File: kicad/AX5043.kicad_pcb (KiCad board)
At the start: 2 copper layers, 43 x 34 mm, 29 parts, among them U1 AX5043, X1 12.000MHz, X2 SMA

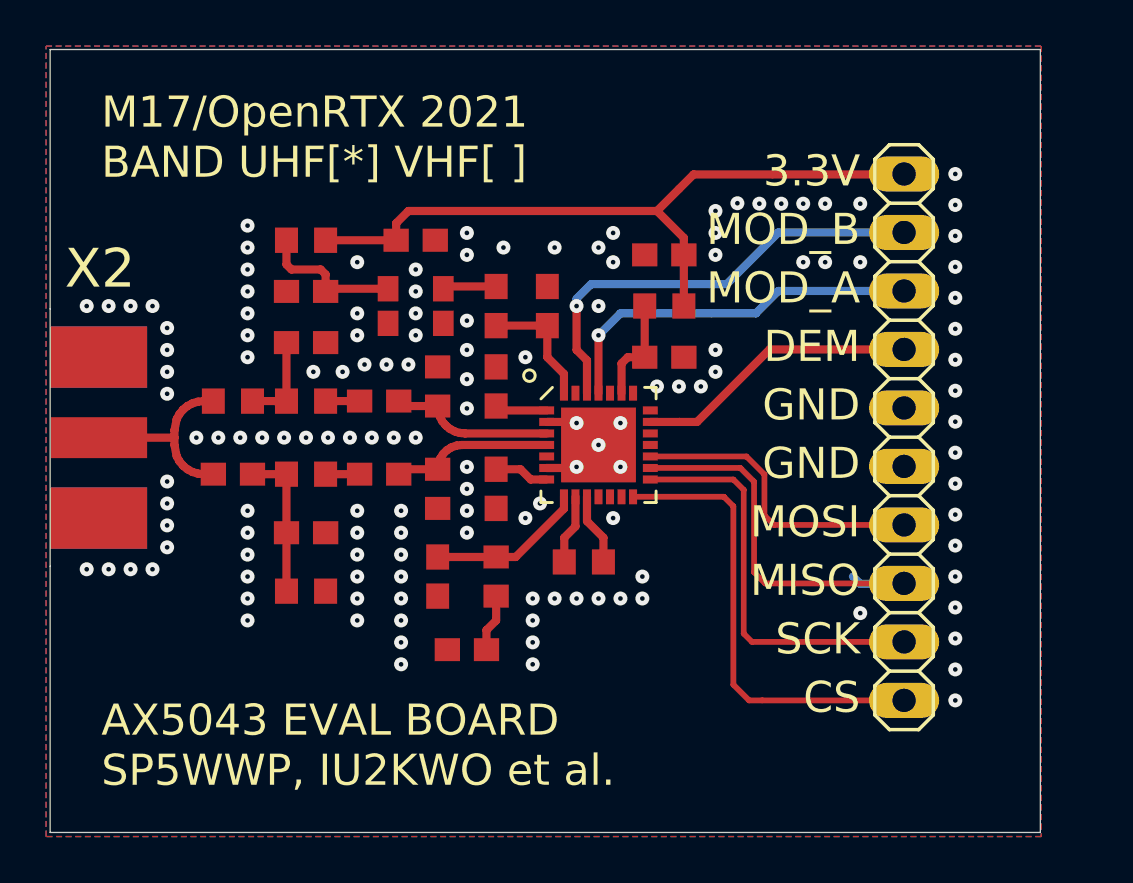
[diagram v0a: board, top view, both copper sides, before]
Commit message: Add rounded corners
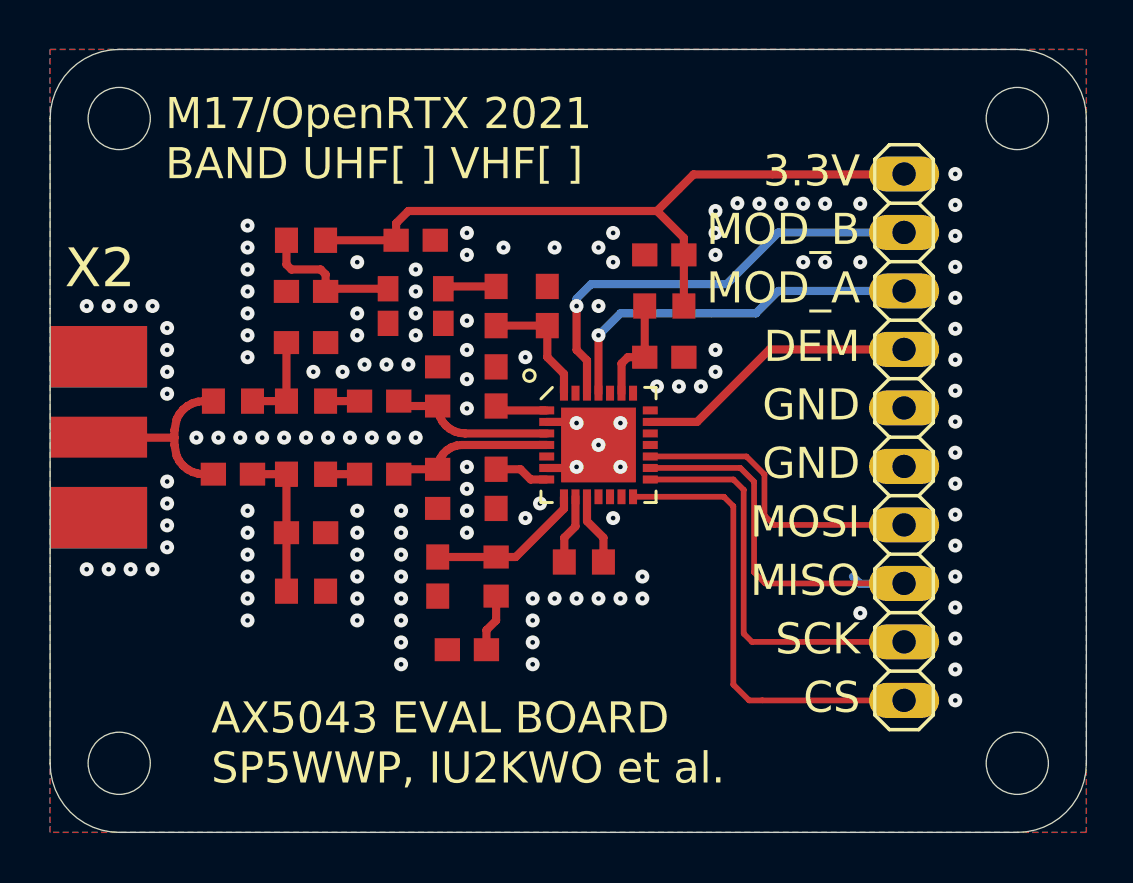
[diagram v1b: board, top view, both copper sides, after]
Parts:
- added REF**: MountingHole_2.7mm_M2.5, MountingHole:MountingHole_2.7mm_M2.5, F.Cu at (169.0, 119.0)
- added REF**: MountingHole_2.7mm_M2.5, MountingHole:MountingHole_2.7mm_M2.5, F.Cu at (169.0, 91.0)
- added REF**: MountingHole_2.7mm_M2.5, MountingHole:MountingHole_2.7mm_M2.5, F.Cu at (130.0, 119.0)
- added REF**: MountingHole_2.7mm_M2.5, MountingHole:MountingHole_2.7mm_M2.5, F.Cu at (130.0, 91.0)
- JP1: value (none) -> PINHD-1X10
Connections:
- R4 pad 1: Net-(R4-Pad1) -> Net-(C6-Pad2)
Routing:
- net GND: vias 125 -> 117
- net (no net): vias 12 -> 20
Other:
- board size 43 x 34 mm -> 45 x 34 mm
- board text added: "M17/OpenRTX 2021 BAND UHF[ ] VHF[ ]"
- board text removed: "M17/OpenRTX 2021 BAND UHF[*] VHF[ ]"

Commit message: Reorganised KiCad libraries
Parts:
- C1, C10, C11, C12, C13, C14, C15, C2, C3, C4, C5, C6, C7, C8, C9: footprint main:C0603 -> AX5043:C0603
- JP1: footprint main:1X10 -> AX5043:1X10
- R1, R10, R2, R3, R4, R5, R6, R7, R8, R9: footprint main:R0603 -> AX5043:R0603
- U1: footprint main:QFN28-5X5-WITH-CENTER-PAD -> AX5043:QFN28-5X5-WITH-CENTER-PAD
- X1: footprint main:ASE -> AX5043:ASE
- X2: footprint main:J502-ND-142-0711-821_826 -> AX5043:J502-ND-142-0711-821_826

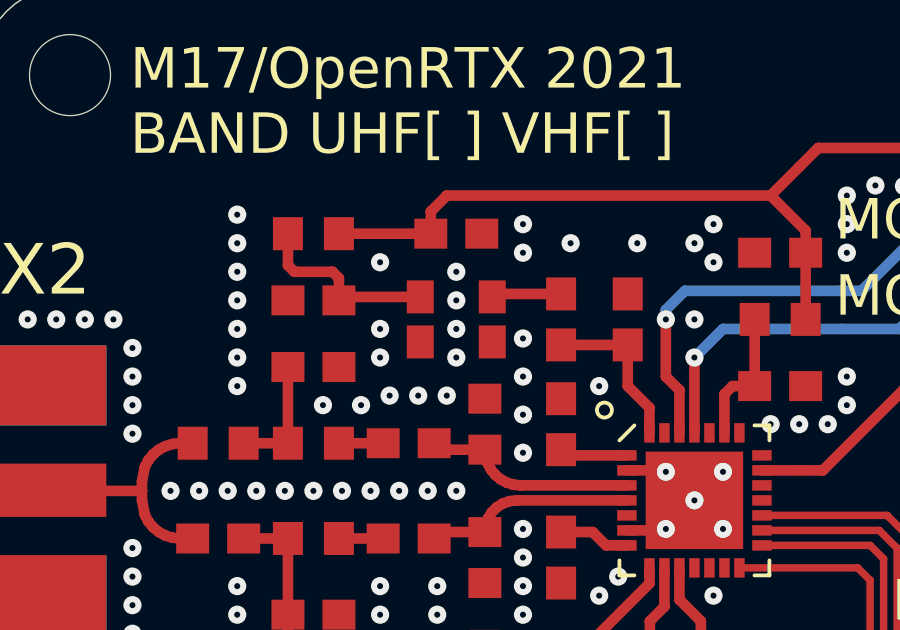
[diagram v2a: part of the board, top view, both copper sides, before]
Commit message: New footprint for TCXO, model is ECS-TXO-2520
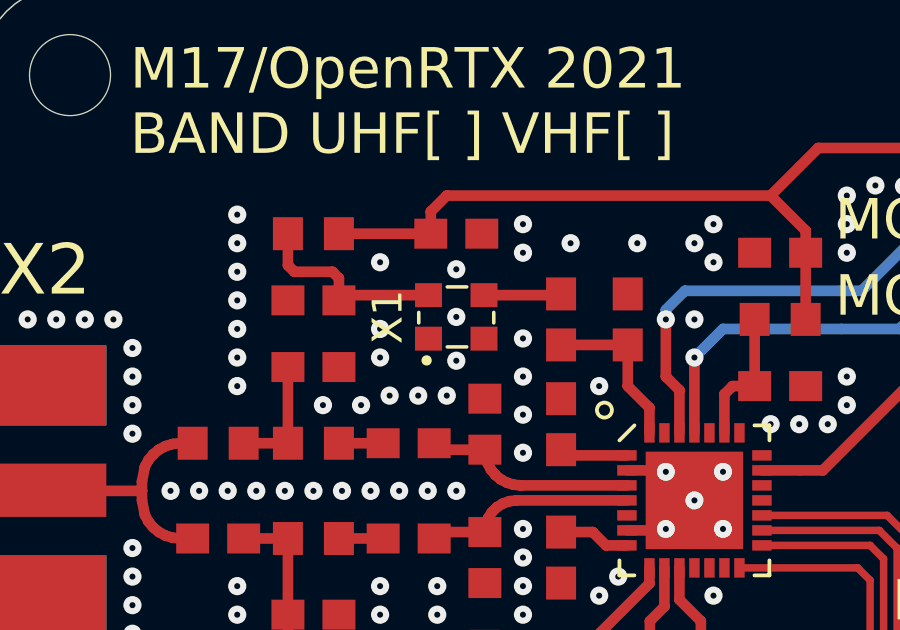
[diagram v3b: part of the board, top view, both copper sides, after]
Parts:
- X1: footprint AX5043:ASE -> AX5043:ECS-TXO-2520
- moved X1 0.08 mm to (142.9, 99.1), turned to 180 degrees
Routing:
- net GND: vias 117 -> 116

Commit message: Gerber files for PCB manufacturing
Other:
- board text added: "M17/OpenRTX 2021 v1.0 BAND UHF[ ] VHF[ ]"
- board text removed: "M17/OpenRTX 2021 BAND UHF[ ] VHF[ ]"

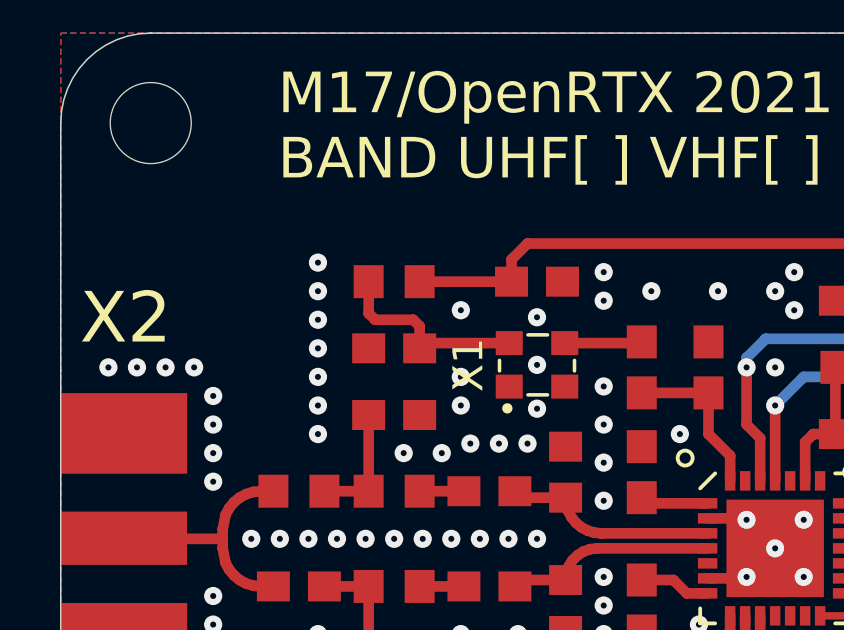
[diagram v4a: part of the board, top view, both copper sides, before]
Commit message: Fixed some unconnected ground vias, re-generated gerber files
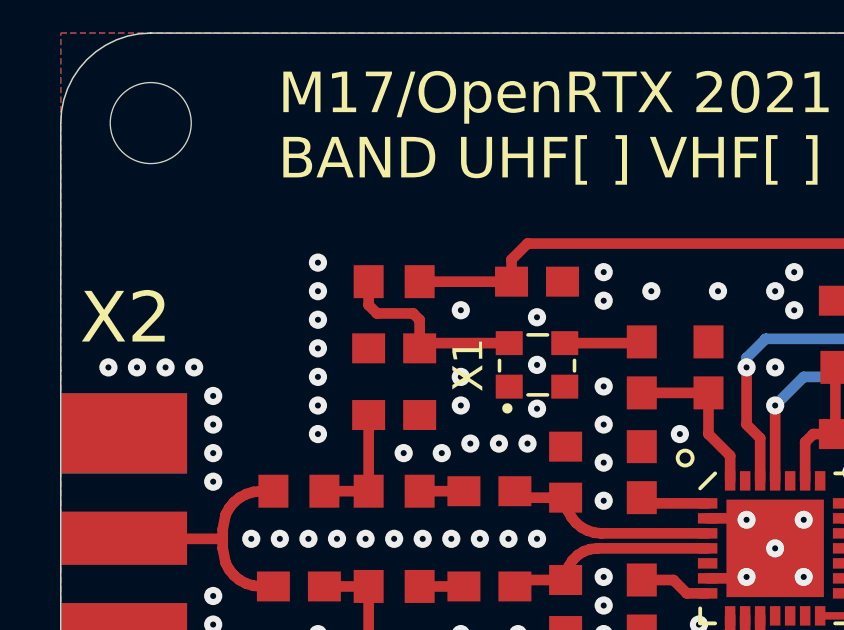
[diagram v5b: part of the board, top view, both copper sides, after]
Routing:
- net GND: vias 116 -> 136
- net (no net): vias 20 -> 0
